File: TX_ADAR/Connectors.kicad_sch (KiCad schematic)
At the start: 4 parts, among them J1 Conn_Coaxial, J11 RJ45_LED_Shielded, J12 RJ45_LED_Shielded, J2 Conn_Coaxial

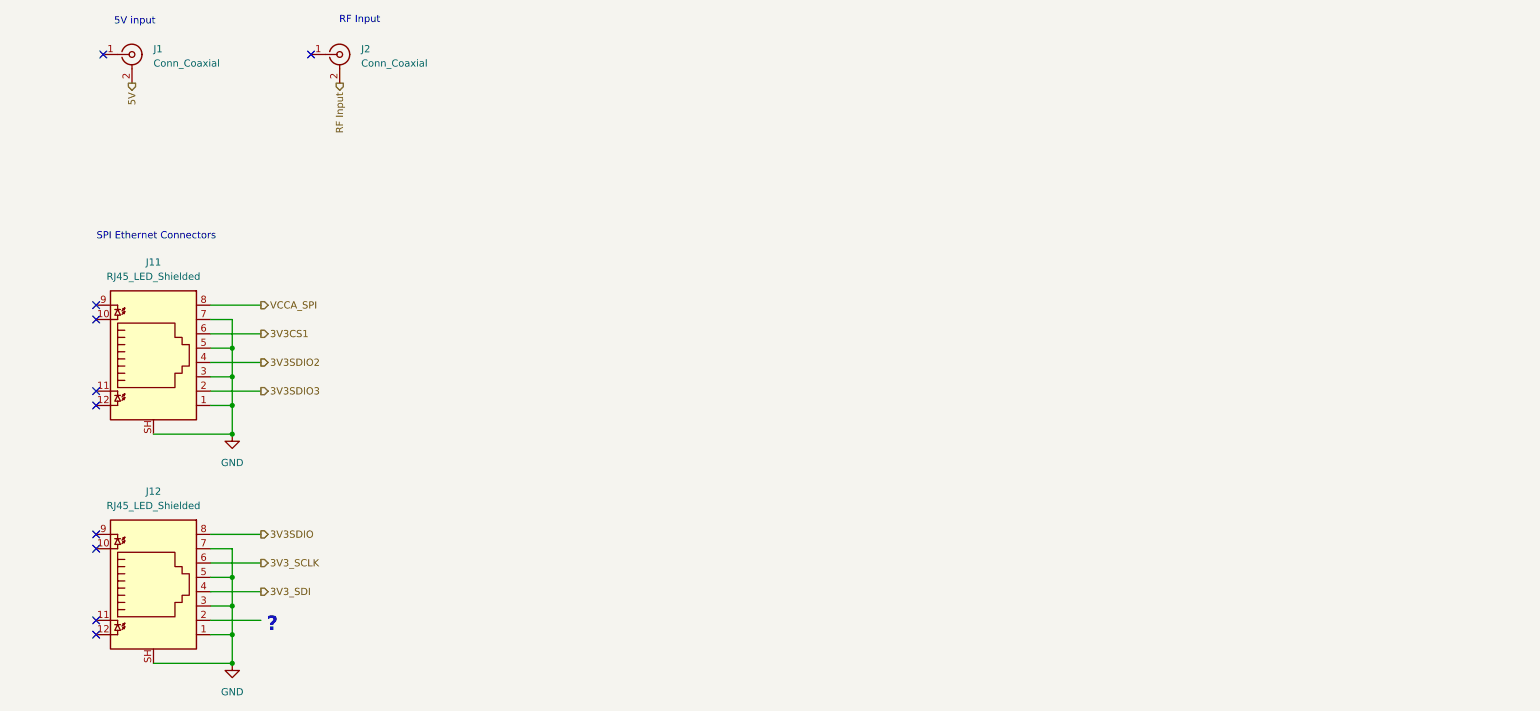
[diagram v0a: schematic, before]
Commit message: Cleaning up schematic
Added Cal Line
Connected RFOuts to connectors
Worked on State Machine connections
Finished connecting SDP Connector (need to double check)
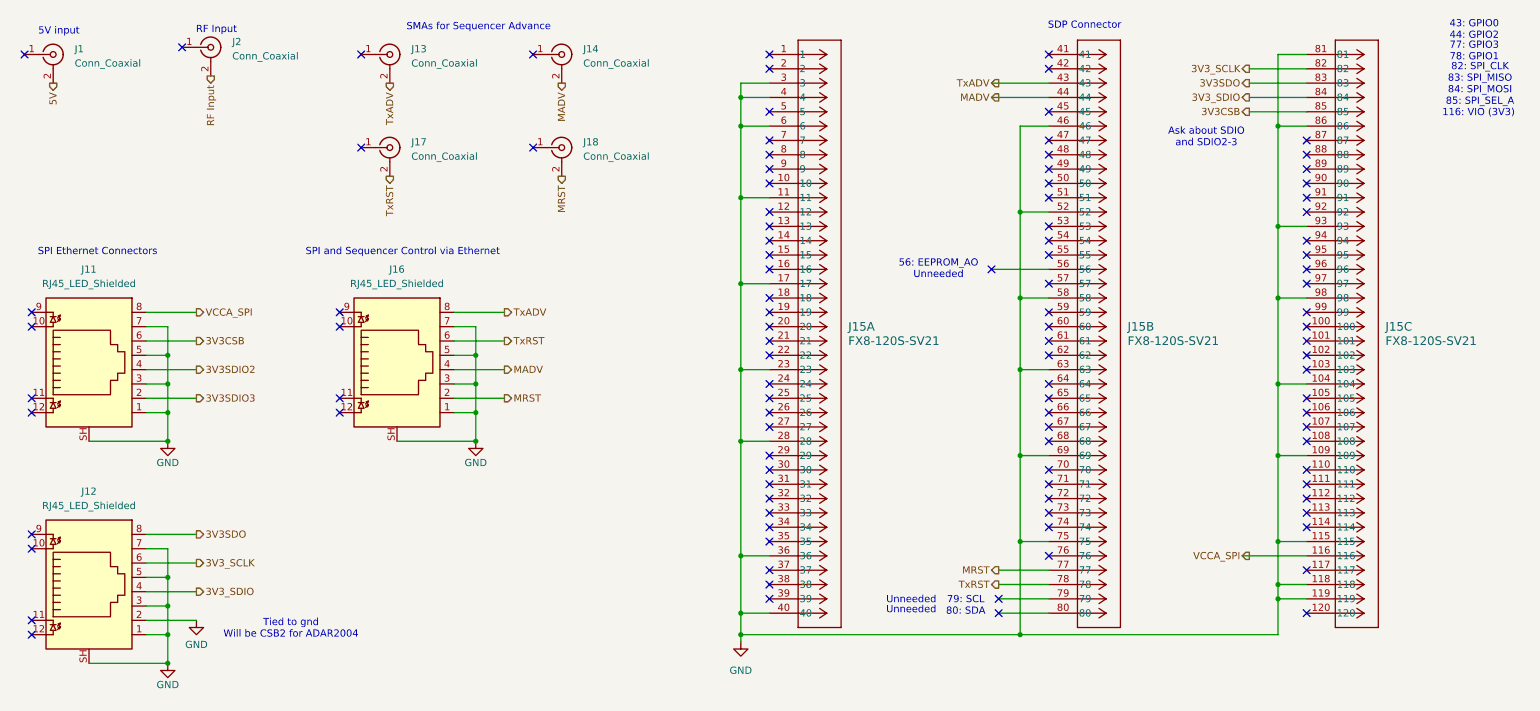
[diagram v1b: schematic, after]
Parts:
- added J13, J14, J17, J18: Conn_Coaxial, symbol Connector:Conn_Coaxial
- added J15: FX8-120S-SV21, CONN120_FX8-120S-SV_HIR, symbol 2026-08-26_15-47-23:FX8-120S-SV21
- added J16: RJ45_LED_Shielded, symbol Connector:RJ45_LED_Shielded
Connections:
- net 3V3_SCLK: now also J15.82
- net GND: now also J12.2, J15.104, J15.109, J15.11, J15.115, J15.118, J15.119, J15.17, J15.23, J15.28, J15.3, J15.36, J15.4, J15.40, J15.46, J15.52, J15.58, J15.6, J15.63, J15.69, J15.75, J15.81, J15.86, J15.93, J15.98, J16.1, J16.3, J16.5, J16.7, J16.SH
- net VCCA_SPI: now also J15.116
- net 3V3CS1 renamed 3V3CSB
- net 3V3CSB: now also J15.85
- net 3V3SDIO renamed 3V3SDO
- net 3V3SDO: now also J15.83
- net 3V3_SDI renamed 3V3_SDIO
- net 3V3_SDIO: now also J15.84
- new net MADV: J14.2 (Ext), J15.44, J16.4
- new net MRST: J15.77, J16.2, J18.2 (Ext)
- new net TxADV: J13.2 (Ext), J15.43, J16.8
- new net TxRST: J15.78, J16.6, J17.2 (Ext)
- no-connect marks 10 -> 105
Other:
- note added: "116: VIO (3V3)"
- note added: "43: GPIO0 44: GPIO2"
- note added: "56: EEPROM_AO"
- note added: "77: GPIO3 78: GPIO1"
- note added: "79: SCL 80: SDA"
- note added: "82: SPI_CLK 83: SPI_MISO 84: SPI_MOSI 85: SPI_SEL_A"
- note added: "Ask about SDIO and SDIO2-3"
- note added: "SDP Connector"
- note added: "SMAs for Sequencer Advance"
- note added: "SPI and Sequencer Control via Ethernet"
- note added: "Tied to gnd Will be CSB2 for ADAR2004"
- note added: "Unneeded"
- note removed: "?"
- moved on the sheet: J1, J11, J12, J2

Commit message: Running ERC
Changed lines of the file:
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@@
+	)
+	(junction
+		(at 40.64 66.04)
+		(diameter 0)
+		(color 0 0 0 0)
 	)
 	(junction
@@
 	(wire
 		(pts
-			(xy 35.56 66.04) (xy 44.45 66.04)
+			(xy 35.56 66.04) (xy 40.64 66.04)
 		)
 		(stroke
@@
 	(wire
 		(pts
+			(xy 40.64 66.04) (xy 44.45 66.04)
+		)
+		(stroke
+			(width 0)
+			(type default)
+		)
+	)
+	(wire
+		(pts
 			(xy 146.05 45.72) (xy 140.97 45.72)
 		)
@@
 		)
 	)
+	(hierarchical_label "3V3SDO"
+		(shape output)
+		(at 231.14 25.4 180)
+		(effects
+			(font
+				(size 1.27 1.27)
+			)
+			(justify right)
+		)
+	)
+	(hierarchical_label "TxRST"
+		(shape output)
+		(at 99.06 71.12 0)
+		(effects
+			(font
+				(size 1.27 1.27)
+			)
+			(justify left)
+		)
+	)
 	(hierarchical_label "VCCA_SPI"
 		(shape output)
@@
 		)
 	)
-	(hierarchical_label "3V3SDO"
-		(shape output)
-		(at 231.14 25.4 180)
+	(hierarchical_label "TxADV"
+		(shape output)
+		(at 99.06 66.04 0)
+		(effects
+			(font
+				(size 1.27 1.27)
+			)
+			(justify left)
+		)
+	)
+	(hierarchical_label "MADV"
+		(shape output)
+		(at 99.06 76.2 0)
+		(effects
+			(font
+				(size 1.27 1.27)
+			)
+			(justify left)
+		)
+	)
+	(hierarchical_label "TxRST"
+		(shape output)
+		(at 78.74 41.91 270)
 		(effects
 			(font
@@
 		)
 	)
-	(hierarchical_label "TxRST"
-		(shape output)
-		(at 99.06 71.12 0)
+	(hierarchical_label "MADV"
+		(shape output)
+		(at 109.22 25.4 270)
+		(effects
+			(font
+				(size 1.27 1.27)
+			)
+			(justify right)
+		)
+	)
+	(hierarchical_label "3V3_SCLK"
+		(shape output)
+		(at 44.45 110.49 0)
 		(effects
 			(font
@@
 		)
 	)
-	(hierarchical_label "TxADV"
-		(shape output)
-		(at 99.06 66.04 0)
-		(effects
-			(font
-				(size 1.27 1.27)
-			)
-			(justify left)
+	(hierarchical_label "VCCA_SPI"
+		(shape output)
+		(at 229.87 109.22 180)
+		(effects
+			(font
+				(size 1.27 1.27)
+			)
+			(justify right)
 		)
 	)
 	(hierarchical_label "MADV"
 		(shape output)
-		(at 99.06 76.2 0)
-		(effects
-			(font
-				(size 1.27 1.27)
-			)
-			(justify left)
-		)
-	)
-	(hierarchical_label "TxRST"
-		(shape output)
-		(at 78.74 41.91 270)
+		(at 186.69 27.94 180)
 		(effects
 			(font
@@
 		)
 	)
-	(hierarchical_label "MADV"
-		(shape output)
-		(at 109.22 25.4 270)
-		(effects
-			(font
-				(size 1.27 1.27)
-			)
-			(justify right)
-		)
-	)
-	(hierarchical_label "3V3_SCLK"
-		(shape output)
-		(at 44.45 110.49 0)
-		(effects
-			(font
-				(size 1.27 1.27)
-			)
-			(justify left)
-		)
-	)
-	(hierarchical_label "MADV"
-		(shape output)
-		(at 186.69 27.94 180)
-		(effects
-			(font
-				(size 1.27 1.27)
-			)
-			(justify right)
-		)
-	)
 	(hierarchical_label "MRST"
 		(shape output)
 		(at 109.22 41.91 270)
-		(effects
-			(font
-				(size 1.27 1.27)
-			)
-			(justify right)
-		)
-	)
-	(hierarchical_label "VCCA_SPI"
-		(shape output)
-		(at 231.14 109.22 180)
 		(effects
 			(font
@@
 					(unit 1)
 				)
+			)
+		)
+	)
+	(symbol
+		(lib_id "power:PWR_FLAG")
+		(at 40.64 66.04 0)
+		(unit 1)
+		(body_style 1)
+		(exclude_from_sim no)
+		(in_bom yes)
+		(on_board yes)
+		(in_pos_files yes)
+		(dnp no)
+		(fields_autoplaced yes)
+		(property "Reference" "#FLG03"
+			(at 40.64 64.135 0)
+			(hide yes)
+			(show_name no)
+			(do_not_autoplace no)
+			(effects
+				(font
+					(size 1.27 1.27)
+				)
+			)
+		)
+		(property "Value" "PWR_FLAG"
+			(at 40.64 60.96 0)
+			(hide yes)
+			(show_name no)
+			(do_not_autoplace no)
+			(effects
+				(font
+					(size 1.27 1.27)
+				)
+			)
+		)
+		(property "Footprint" ""
+			(at 40.64 66.04 0)
+			(hide yes)
+			(show_name no)
+			(do_not_autoplace no)
+			(effects
+				(font
+					(size 1.27 1.27)
+				)
+			)
+		)
+		(property "Datasheet" ""
+			(at 40.64 66.04 0)
+			(hide yes)
+			(show_name no)
+			(do_not_autoplace no)
+			(effects
+				(font
+					(size 1.27 1.27)
+				)
+			)
+		)
+		(property "Description" "Special symbol for telling ERC where power comes from"
+			(at 40.64 66.04 0)
+			(hide yes)
+			(show_name no)
+			(do_not_autoplace no)
+			(effects
+				(font
+					(size 1.27 1.27)
+				)
+			)
+		)
+		(pin "1"
+		)
+		(instances
+			(project "TX_ADAR"
+				(path "/5bb7bcfe-c6dc-48dd-b109-2cc47fd52212/5711866b-ad81-4828-9e56-17f3c1154618"
+					(reference "#FLG03")
+					(unit 1)
+				)

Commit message: Fixing problems pointed out
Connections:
- net 5V: now also J1.1 (In); no longer J1.2 (Ext)
- net GND: now also J1.2 (Ext), J13.2 (Ext), J14.2 (Ext), J17.2 (Ext), J18.2 (Ext), J2.1 (In)
- net MADV: now also J14.1 (In); no longer J14.2 (Ext)
- net MRST: now also J18.1 (In); no longer J18.2 (Ext)
- net TxADV: now also J13.1 (In); no longer J13.2 (Ext)
- net TxRST: now also J17.1 (In); no longer J17.2 (Ext)
- no-connect marks 105 -> 99
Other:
- moved on the sheet: J1, J13, J14, J17, J18, J2

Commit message: Fixed more issues
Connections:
- net GND: now also J2.2 (Ext); no longer J2.1 (In)
- net RF Input: now also J2.1 (In); no longer J2.2 (Ext)
- net 5V renamed +5V
- net VCCA_SPI renamed 3V3_VCCB_SPI
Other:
- moved on the sheet: J2
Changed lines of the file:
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@@
 	(text "RF Input"
 		(exclude_from_sim no)
-		(at 56.896 16.002 0)
+		(at 58.166 16.002 0)
 		(effects
 			(font
@@
 	(wire
 		(pts
-			(xy 46.99 19.05) (xy 50.8 19.05)
+			(xy 140.97 109.22) (xy 140.97 88.9)
 		)
 		(stroke
@@
 	(wire
 		(pts
-			(xy 140.97 109.22) (xy 140.97 88.9)
+			(xy 90.17 81.28) (xy 99.06 81.28)
 		)
 		(stroke
@@
 	(wire
 		(pts
-			(xy 90.17 81.28) (xy 99.06 81.28)
+			(xy 13.97 19.05) (xy 16.51 19.05)
 		)
 		(stroke
@@
 		)
 	)
-	(hierarchical_label "5V"
-		(shape output)
-		(at 16.51 19.05 180)
-		(effects
-			(font
-				(size 1.27 1.27)
-			)
-			(justify right)
-		)
-	)
 	(hierarchical_label "MRST"
 		(shape output)
@@
 		)
 	)
-	(hierarchical_label "VCCA_SPI"
+	(hierarchical_label "3V3_VCCB_SPI"
 		(shape output)
 		(at 44.45 66.04 0)
@@
 		)
 	)
-	(hierarchical_label "VCCA_SPI"
+	(hierarchical_label "3V3_VCCB_SPI"
 		(shape output)
 		(at 229.87 109.22 180)
@@
 		)
 	)
+	(hierarchical_label "RF Input"
+		(shape output)
+		(at 52.07 19.05 180)
+		(effects
+			(font
+				(size 1.27 1.27)
+			)
+			(justify right)
+		)
+	)
 	(hierarchical_label "MADV"
 		(shape output)
@@
 		)
 	)
-	(hierarchical_label "RF Input"
-		(shape output)
-		(at 55.88 24.13 270)
-		(effects
-			(font
-				(size 1.27 1.27)
-			)
-			(justify right)
-		)
-	)
 	(hierarchical_label "3V3_SDIO"
 		(shape output)
@@
 	)
 	(symbol
-		(lib_id "power:GND")
-		(at 111.76 31.75 0)
-		(unit 1)
-		(body_style 1)
-		(exclude_from_sim no)
-		(in_bom yes)
-		(on_board yes)
-		(in_pos_files yes)
-		(dnp no)
-		(fields_autoplaced yes)
-		(property "Reference" "#PWR015"
-			(at 111.76 38.1 0)
-			(hide yes)
-			(show_name no)
-			(do_not_autoplace no)
-			(effects
-				(font
-					(size 1.27 1.27)
-				)
-			)
-		)
-		(property "Value" "GND"
-			(at 111.76 36.83 0)
-			(show_name no)
-			(do_not_autoplace no)
-			(effects
-				(font
-					(size 1.27 1.27)
-				)
-			)
-		)
-		(property "Footprint" ""
-			(at 111.76 31.75 0)
-			(hide yes)
-			(show_name no)
-			(do_not_autoplace no)
-			(effects
-				(font
-					(size 1.27 1.27)
-				)
-			)
-		)
-		(property "Datasheet" ""
-			(at 111.76 31.75 0)
-			(hide yes)
-			(show_name no)
-			(do_not_autoplace no)
-			(effects
-				(font
-					(size 1.27 1.27)
-				)
-			)
-		)
-		(property "Description" "Power symbol creates a global label with name \"GND\" , ground"
-			(at 111.76 31.75 0)
-			(hide yes)
-			(show_name no)
-			(do_not_autoplace no)
-			(effects
-				(font
-					(size 1.27 1.27)
-				)
-			)
-		)
-		(pin "1"
-		)
-		(instances
-			(project "TX_ADAR"
-				(path "/5bb7bcfe-c6dc-48dd-b109-2cc47fd52212/5711866b-ad81-4828-9e56-17f3c1154618"
-					(reference "#PWR015")
-					(unit 1)
-				)
-			)
-		)
-	)
-	(symbol
 		(lib_id "2026-08-26_15-47-23:FX8-120S-SV21")
 		(at 146.05 20.32 0)
@@
 	)
 	(symbol
-		(lib_id "power:GND")
-		(at 46.99 19.05 0)
-		(unit 1)
-		(body_style 1)
-		(exclude_from_sim no)
-		(in_bom yes)
-		(on_board yes)
-		(in_pos_files yes)
-		(dnp no)
-		(property "Reference" "#PWR010"
-			(at 46.99 25.4 0)
-			(hide yes)
-			(show_name no)
-			(do_not_autoplace no)
-			(effects
-				(font
-					(size 1.27 1.27)
-				)
-			)
-		)
-		(property "Value" "GND"
-			(at 46.99 22.86 0)
-			(show_name no)
-			(do_not_autoplace no)
-			(effects
-				(font
-					(size 1.27 1.27)
-				)
-			)
-		)
-		(property "Footprint" ""
-			(at 46.99 19.05 0)
-			(hide yes)
-			(show_name no)
-			(do_not_autoplace no)
-			(effects
-				(font
-					(size 1.27 1.27)
-				)
-			)
-		)
-		(property "Datasheet" ""
-			(at 46.99 19.05 0)
-			(hide yes)
-			(show_name no)
-			(do_not_autoplace no)
-			(effects
-				(font
-					(size 1.27 1.27)
-				)
-			)
-		)
-		(property "Description" "Power symbol creates a global label with name \"GND\" , ground"
-			(at 46.99 19.05 0)
-			(hide yes)
-			(show_name no)
-			(do_not_autoplace no)
-			(effects
-				(font
-					(size 1.27 1.27)
-				)
-			)
-		)
-		(pin "1"
-		)
-		(instances
-			(project "TX_ADAR"
-				(path "/5bb7bcfe-c6dc-48dd-b109-2cc47fd52212/5711866b-ad81-4828-9e56-17f3c1154618"
-					(reference "#PWR010")
-					(unit 1)
-				)
-			)
-		)
-	)
-	(symbol
 		(lib_id "2026-08-26_15-47-23:FX8-120S-SV21")
 		(at 241.3 20.32 0)
@@
 	(symbol
 		(lib_id "Connector:Conn_Coaxial")
-		(at 55.88 19.05 0)
+		(at 57.15 19.05 0)
 		(unit 1)
 		(body_style 1)
@@
 		(fields_autoplaced yes)
 		(property "Reference" "J2"
-			(at 59.69 18.0731 0)
+			(at 60.96 18.0731 0)
 			(show_name no)
 			(do_not_autoplace no)
@@
 		)
 		(property "Value" "Conn_Coaxial"
-			(at 59.69 20.6131 0)
+			(at 60.96 20.6131 0)
 			(show_name no)
 			(do_not_autoplace no)
@@
 		)
 		(property "Footprint" ""
-			(at 55.88 19.05 0)
+			(at 57.15 19.05 0)
 			(hide yes)
 			(show_name no)
@@
 		)
 		(property "Datasheet" ""
-			(at 55.88 19.05 0)
+			(at 57.15 19.05 0)
 			(hide yes)
 			(show_name no)
@@
 		)
 		(property "Description" "coaxial connector (BNC, SMA, SMB, SMC, Cinch/RCA, LEMO, ...)"
-			(at 55.88 19.05 0)
+			(at 57.15 19.05 0)
 			(hide yes)
 			(show_name no)
@@
 	(symbol
 		(lib_id "power:GND")
+		(at 57.15 24.13 0)
+		(unit 1)
+		(body_style 1)
+		(exclude_from_sim no)
+		(in_bom yes)
+		(on_board yes)
+		(in_pos_files yes)
+		(dnp no)
+		(property "Reference" "#PWR010"
+			(at 57.15 30.48 0)
+			(hide yes)
+			(show_name no)
+			(do_not_autoplace no)
+			(effects
+				(font
+					(size 1.27 1.27)
+				)
+			)
+		)
+		(property "Value" "GND"
+			(at 57.15 27.94 0)
+			(show_name no)
+			(do_not_autoplace no)
+			(effects
+				(font
+					(size 1.27 1.27)
+				)
+			)
+		)
+		(property "Footprint" ""
+			(at 57.15 24.13 0)
+			(hide yes)
+			(show_name no)
+			(do_not_autoplace no)
+			(effects
+				(font
+					(size 1.27 1.27)
+				)
+			)
+		)
+		(property "Datasheet" ""
+			(at 57.15 24.13 0)
+			(hide yes)
+			(show_name no)
+			(do_not_autoplace no)
+			(effects
+				(font
+					(size 1.27 1.27)
+				)
+			)
+		)
+		(property "Description" "Power symbol creates a global label with name \"GND\" , ground"
+			(at 57.15 24.13 0)
+			(hide yes)
+			(show_name no)
+			(do_not_autoplace no)
+			(effects
+				(font
+					(size 1.27 1.27)
+				)
+			)
+		)
+		(pin "1"
+		)
+		(instances
+			(project "TX_ADAR"
+				(path "/5bb7bcfe-c6dc-48dd-b109-2cc47fd52212/5711866b-ad81-4828-9e56-17f3c1154618"
+					(reference "#PWR010")
+					(unit 1)
+				)
+			)
+		)
+	)
+	(symbol
+		(lib_id "power:GND")
 		(at 44.45 120.65 0)
 		(unit 1)
@@
 				)
 			)
+		)
+	)
+	(symbol
+		(lib_id "power:+5V")
+		(at 13.97 19.05 0)
+		(unit 1)
+		(body_style 1)
+		(exclude_from_sim no)
+		(in_bom yes)
+		(on_board yes)
+		(in_pos_files yes)
+		(dnp no)
+		(property "Reference" "#PWR053"
+			(at 13.97 22.86 0)
+			(hide yes)
+			(show_name no)
+			(do_not_autoplace no)
+			(effects
+				(font
+					(size 1.27 1.27)
+				)
+			)
+		)
+		(property "Value" "+5V"
+			(at 13.97 14.478 0)
+			(show_name no)
+			(do_not_autoplace no)
+			(effects
+				(font
+					(size 1.27 1.27)
+				)
+			)
+		)
+		(property "Footprint" ""
+			(at 13.97 19.05 0)
+			(hide yes)
+			(show_name no)
+			(do_not_autoplace no)
+			(effects
+				(font
+					(size 1.27 1.27)
+				)
+			)
+		)
+		(property "Datasheet" ""
+			(at 13.97 19.05 0)
+			(hide yes)
+			(show_name no)
+			(do_not_autoplace no)
+			(effects
+				(font
+					(size 1.27 1.27)
+				)
+			)
+		)
+		(property "Description" "Power symbol creates a global label with name \"+5V\""
+			(at 13.97 19.05 0)
+			(hide yes)
+			(show_name no)
+			(do_not_autoplace no)
+			(effects
+				(font
+					(size 1.27 1.27)
+				)
+			)
+		)
+		(pin "1"
+		)
+		(instances
+			(project "TX_ADAR"
+				(path "/5bb7bcfe-c6dc-48dd-b109-2cc47fd52212/5711866b-ad81-4828-9e56-17f3c1154618"
+					(reference "#PWR053")
+					(unit 1)
+				)
+			)
